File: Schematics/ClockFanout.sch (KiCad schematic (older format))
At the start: 38 parts, among them CN401 COAX, CN402 COAX, CN403 COAX, CN404 COAX, CN405 COAX, CN406 COAX, CN407 COAX, CN408 COAX, U401 NB3L553, U402 NB3L553

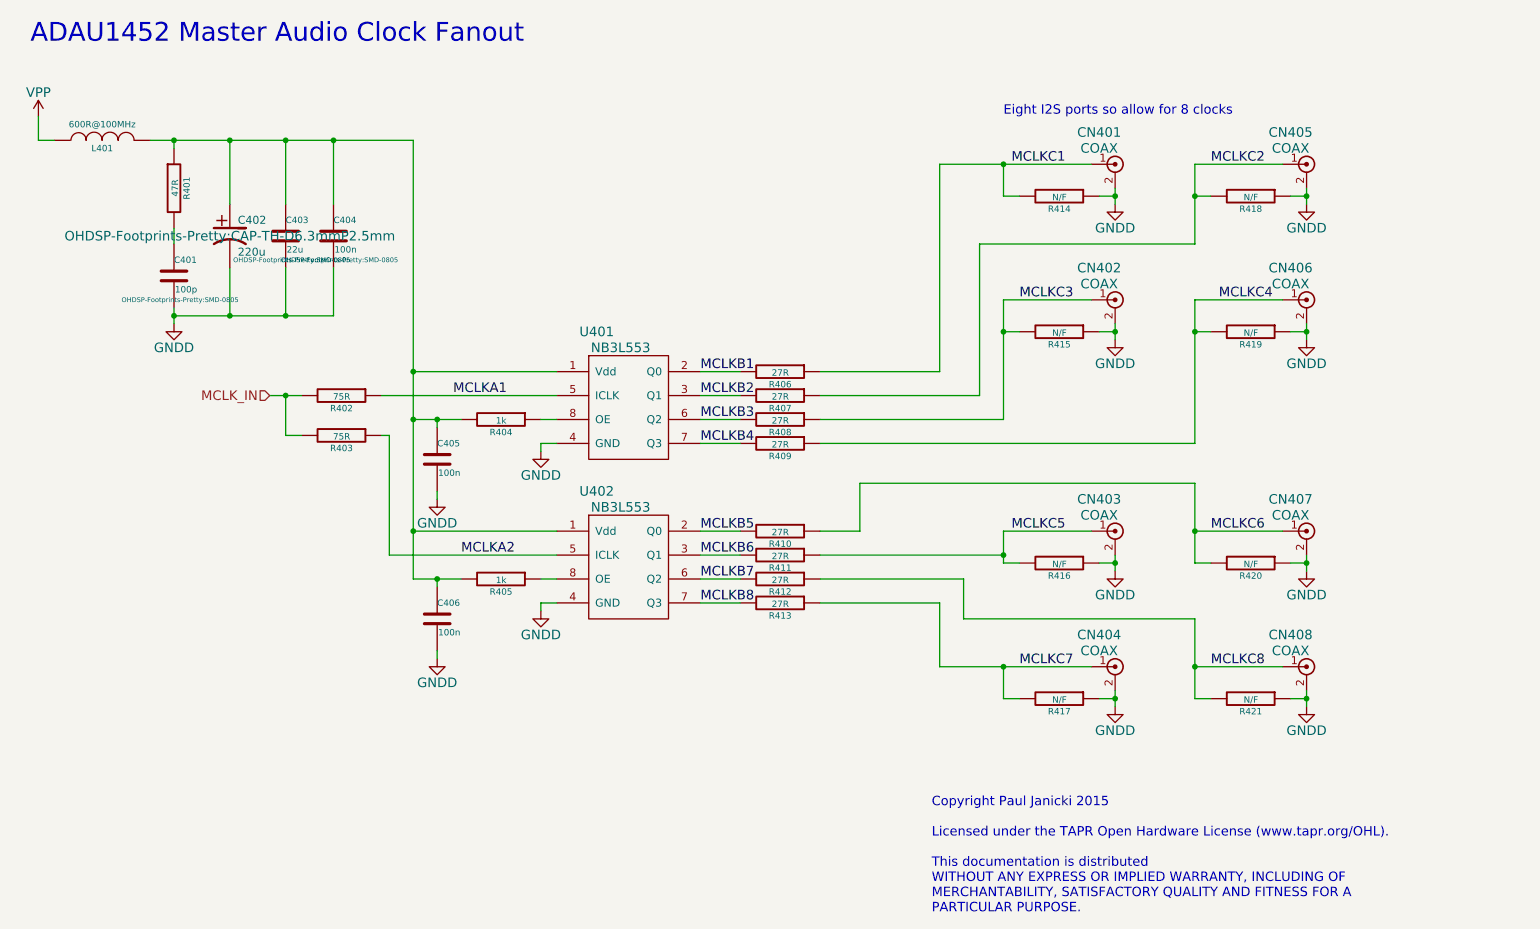
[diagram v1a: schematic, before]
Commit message: Rationalise the clock and clock fan-out schematics.
Rationalise the clock and clock fan-out schematics.
Removed one clock fan out buffer, still have 4 master audio clock
outputs. Also removed local crytsal oscialltor, a low jitter crystal
should perform as well, ADAU1452 has internal "dejittering" anyway.
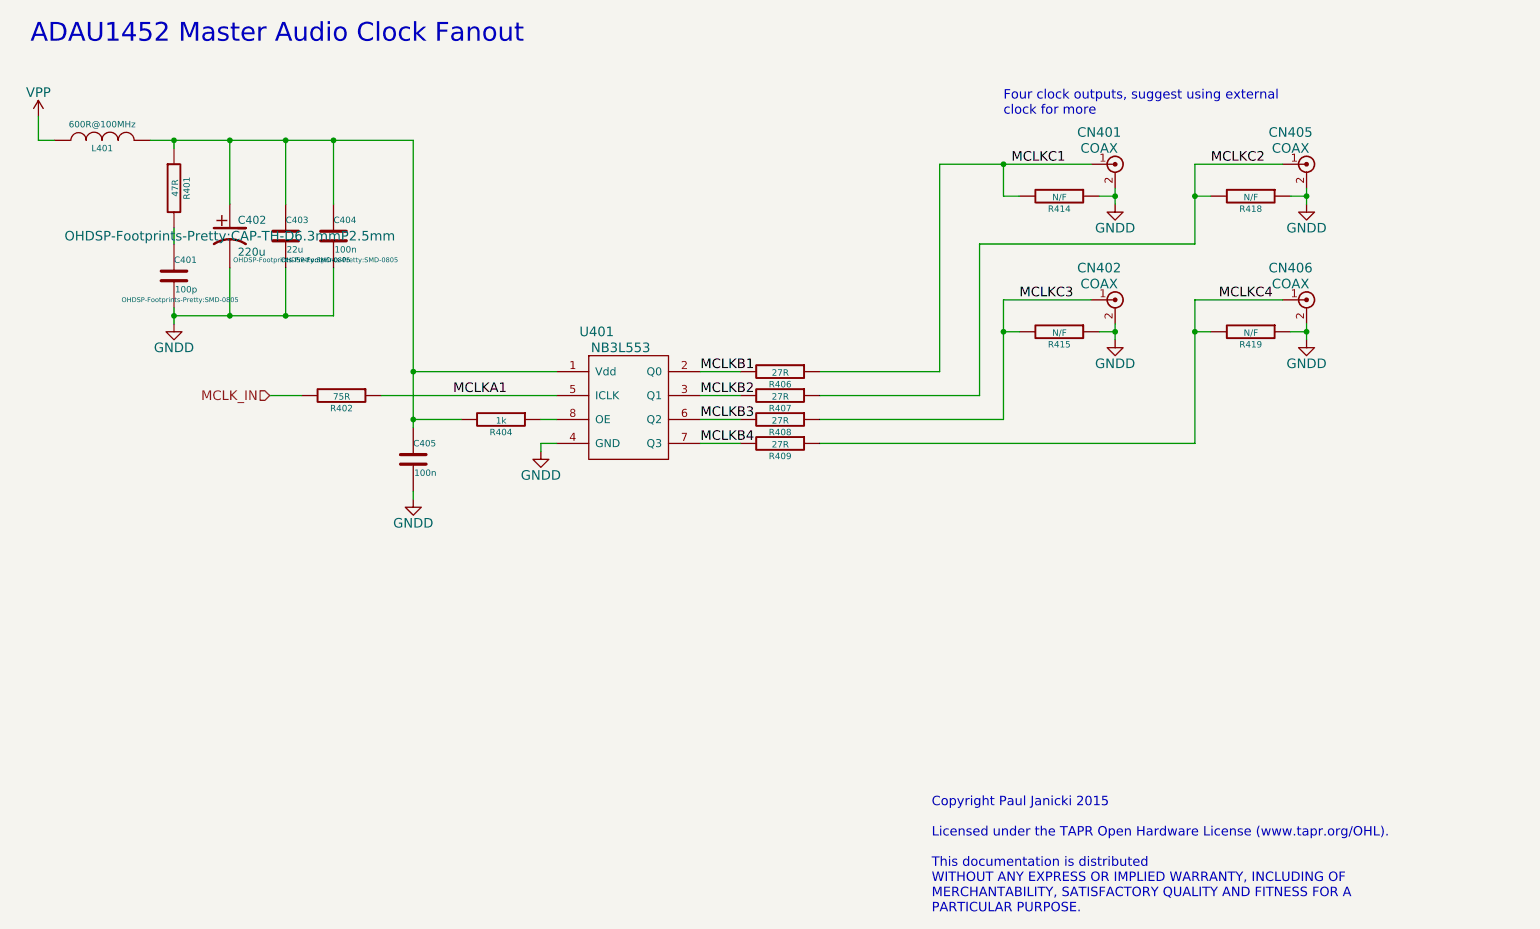
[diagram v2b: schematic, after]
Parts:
- removed C406: 100n, OHDSP-Footprints-Pretty:SMD-0805, symbol C
- removed CN403, CN404, CN407, CN408: COAX, OHDSP-Footprints-Pretty:CONN-RF-UFL, symbol COAX
- removed R403: 75R, OHDSP-Footprints-Pretty:TH-RES-0W25, symbol R
- removed R405: 1k, OHDSP-Footprints-Pretty:SMD-0805, symbol R
- removed R410, R411, R412, R413: 27R, OHDSP-Footprints-Pretty:SMD-0805, symbol R
- removed R416, R417, R420, R421: N/F, OHDSP-Footprints-Pretty:SMD-0805, symbol R
- removed U402: NB3L553, OHDSP-Footprints-Pretty:IC_SOIC_8, symbol IC-CLK-FANOUT-NB3L553
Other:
- note added: "Four clock outputs, suggest using external\nclock for more"
- note removed: "Eight I2S ports so allow for 8 clocks"
- moved on the sheet: C405

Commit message: PCB work, removed a cap
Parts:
- removed C402: 220u, OHDSP-Footprints-Pretty:CAP-TH-D6.3mmP2.5mm, symbol CP1
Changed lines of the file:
@@
-$EndComp
-$Comp
-L CP1 C402
-U 1 1 54E607CF
-P 2600 2850
-F 0 "C402" H 2650 2950 50  0000 L CNN
-F 1 "220u" H 2650 2750 50  0000 L CNN
-F 2 "OHDSP-Footprints-Pretty:CAP-TH-D6.3mmP2.5mm" H 2600 2850 60  0000 C CNN
-F 3 "~" H 2600 2850 60  0000 C CNN
-	1    2600 2850
-	1    0    0    -1
 $EndComp
 $Comp
@@
 Wire Wire Line
 	2250 2800 2250 2900
-Wire Wire Line
-	2600 2250 2600 2650
 Connection ~ 2250 2250
 Wire Wire Line
 	2950 2250 2950 2650
-Connection ~ 2600 2250
 Connection ~ 2950 2250
 Wire Wire Line
@@
 Wire Wire Line
 	2250 3350 3250 3350
-Wire Wire Line
-	2600 3350 2600 3050
 Connection ~ 2250 3350
 Wire Wire Line
 	2950 3350 2950 3050
-Connection ~ 2600 3350
 Connection ~ 2950 3350
 Wire Wire Line

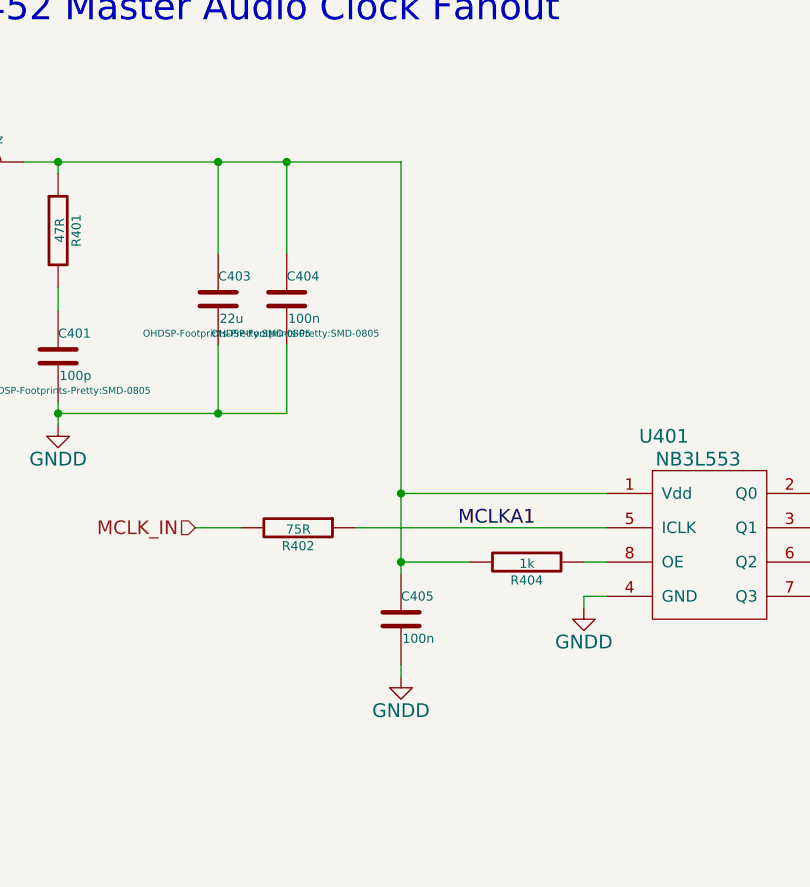
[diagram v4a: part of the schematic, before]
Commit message: PCB Work, minor schematic changes
Removed cap and LED, changed one net label
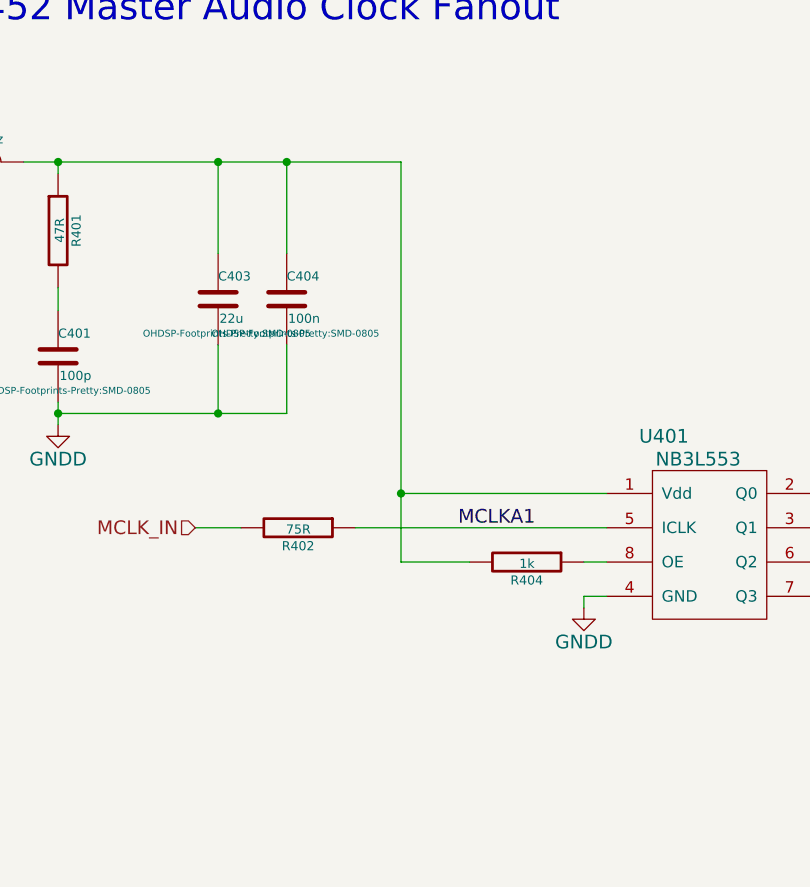
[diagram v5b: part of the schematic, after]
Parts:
- removed C405: 100n, OHDSP-Footprints-Pretty:SMD-0805, symbol C
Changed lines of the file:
@@
 $EndComp
 $Comp
-L GNDD #PWR089
+L GNDD #PWR085
 U 1 1 54E21AA5
 P 4550 4200
-F 0 "#PWR089" H 4550 3950 60  0001 C CNN
+F 0 "#PWR085" H 4550 3950 60  0001 C CNN
 F 1 "GNDD" H 4550 4050 60  0000 C CNN
 F 2 "" H 4550 4200 60  0000 C CNN
 F 3 "" H 4550 4200 60  0000 C CNN
 	1    4550 4200
-	1    0    0    -1
-$EndComp
-$Comp
-L C C405
-U 1 1 54E607C7
-P 3750 4250
-F 0 "C405" H 3750 4350 40  0000 L CNN
-F 1 "100n" H 3756 4165 40  0000 L CNN
-F 2 "OHDSP-Footprints-Pretty:SMD-0805" H 3788 4100 30  0001 C CNN
-F 3 "" H 3750 4250 60  0000 C CNN
-	1    3750 4250
-	1    0    0    -1
-$EndComp
-$Comp
-L GNDD #PWR090
-U 1 1 54E607C8
-P 3750 4500
-F 0 "#PWR090" H 3750 4250 60  0001 C CNN
-F 1 "GNDD" H 3750 4350 60  0000 C CNN
-F 2 "" H 3750 4500 60  0000 C CNN
-F 3 "" H 3750 4500 60  0000 C CNN
-	1    3750 4500
 	1    0    0    -1
 $EndComp
@@
 $EndComp
 $Comp
-L GNDD #PWR091
+L GNDD #PWR086
 U 1 1 54E223FC
 P 8150 2650
-F 0 "#PWR091" H 8150 2400 60  0001 C CNN
+F 0 "#PWR086" H 8150 2400 60  0001 C CNN
 F 1 "GNDD" H 8150 2500 60  0000 C CNN
 F 2 "" H 8150 2650 60  0000 C CNN
@@
 $EndComp
 $Comp
-L GNDD #PWR092
+L GNDD #PWR087
 U 1 1 54E228B4
 P 9350 2650
-F 0 "#PWR092" H 9350 2400 60  0001 C CNN
+F 0 "#PWR087" H 9350 2400 60  0001 C CNN
 F 1 "GNDD" H 9350 2500 60  0000 C CNN
 F 2 "" H 9350 2650 60  0000 C CNN
@@
 Wire Wire Line
 	4550 4150 4650 4150
-Connection ~ 3750 4000
-Wire Wire Line
-	3750 4500 3750 4450
 Wire Wire Line
 	7050 2400 8000 2400
@@
 $EndComp
 $Comp
-L GNDD #PWR093
+L GNDD #PWR088
 U 1 1 54E22C88
 P 8150 3500
-F 0 "#PWR093" H 8150 3250 60  0001 C CNN
+F 0 "#PWR088" H 8150 3250 60  0001 C CNN
 F 1 "GNDD" H 8150 3350 60  0000 C CNN
 F 2 "" H 8150 3500 60  0000 C CNN
@@
 $EndComp
 $Comp
-L GNDD #PWR094
+L GNDD #PWR089
 U 1 1 54E22D69
 P 9350 3500
-F 0 "#PWR094" H 9350 3250 60  0001 C CNN
+F 0 "#PWR089" H 9350 3250 60  0001 C CNN
 F 1 "GNDD" H 9350 3350 60  0000 C CNN
 F 2 "" H 9350 3500 60  0000 C CNN
@@
 $EndComp
 $Comp
-L GNDD #PWR095
+L GNDD #PWR090
 U 1 1 54E607CE
 P 2250 3400
-F 0 "#PWR095" H 2250 3150 60  0001 C CNN
+F 0 "#PWR090" H 2250 3150 60  0001 C CNN
 F 1 "GNDD" H 2250 3250 60  0000 C CNN
 F 2 "" H 2250 3400 60  0000 C CNN
@@
 	1400 2250 1500 2250
 $Comp
-L VPP #PWR096
+L VPP #PWR091
 U 1 1 54E24C37
 P 1400 2100
-F 0 "#PWR096" H 1400 1950 60  0001 C CNN
+F 0 "#PWR091" H 1400 1950 60  0001 C CNN
 F 1 "VPP" H 1400 2250 60  0000 C CNN
 F 2 "" H 1400 2100 60  0000 C CNN
@@
 	3050 3850 2850 3850
 Wire Wire Line
-	3750 2250 3750 4050
+	3750 2250 3750 4000
 $EndSCHEMATC
